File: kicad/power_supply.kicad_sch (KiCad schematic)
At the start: 2 parts

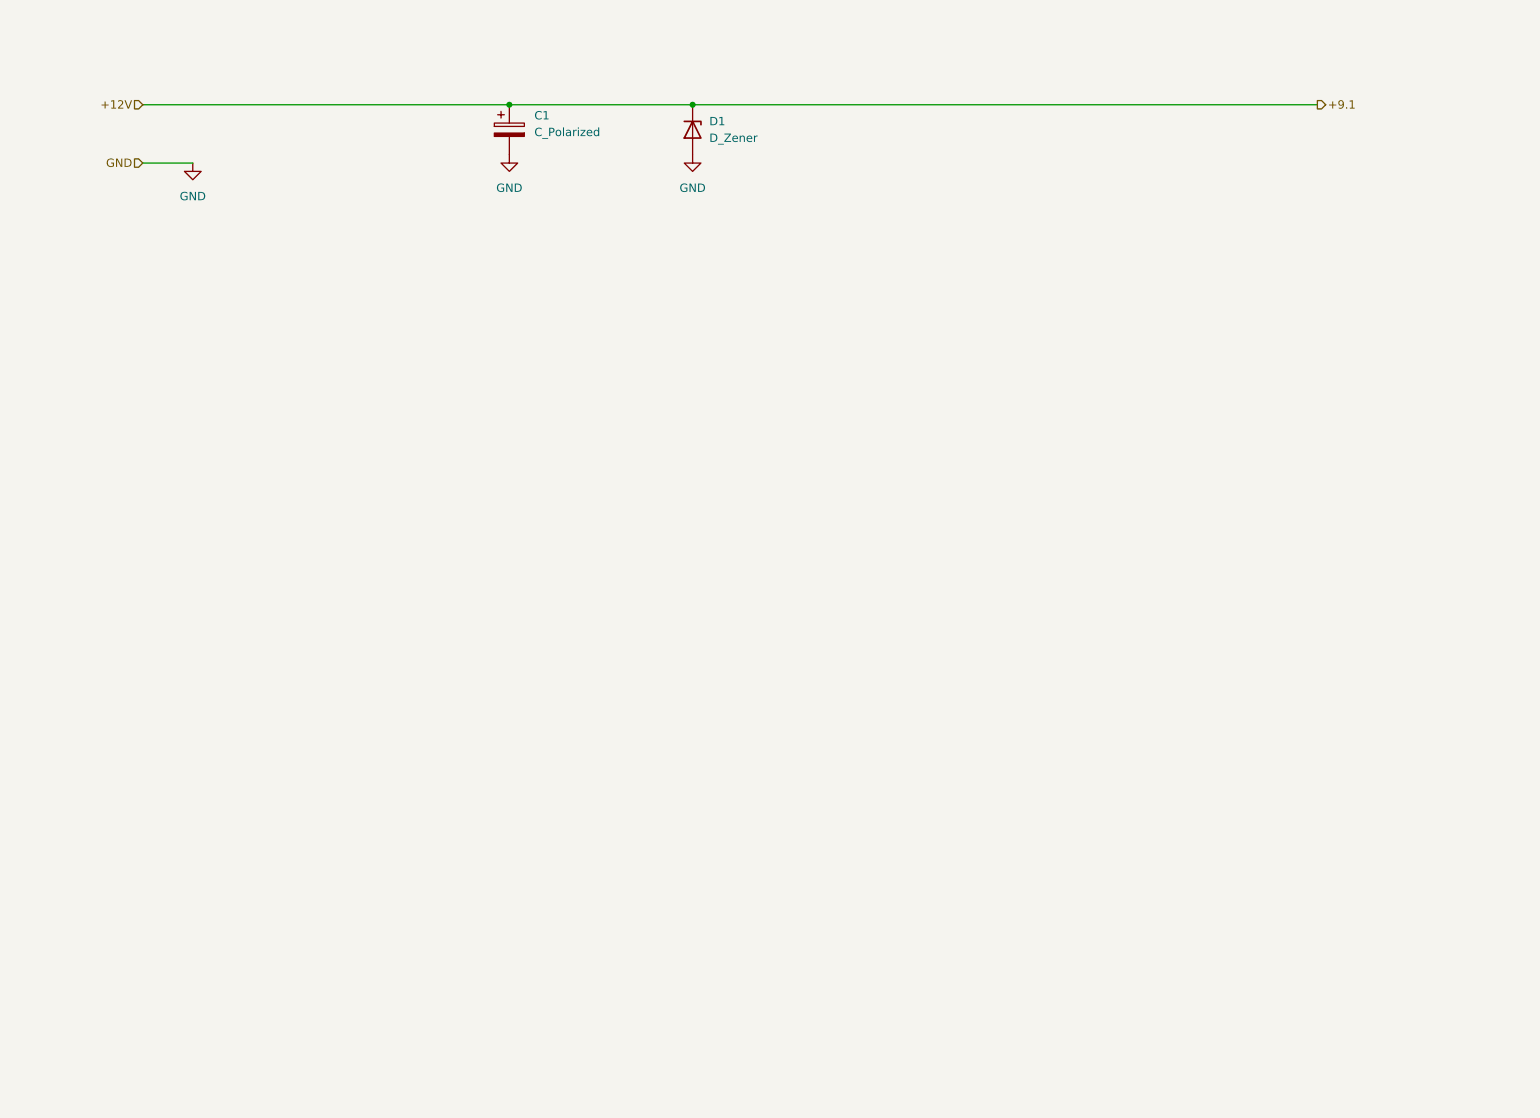
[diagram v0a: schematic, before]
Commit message: modificato lo schema della power supply aggiungendo più LM78xx per le varie tensioni
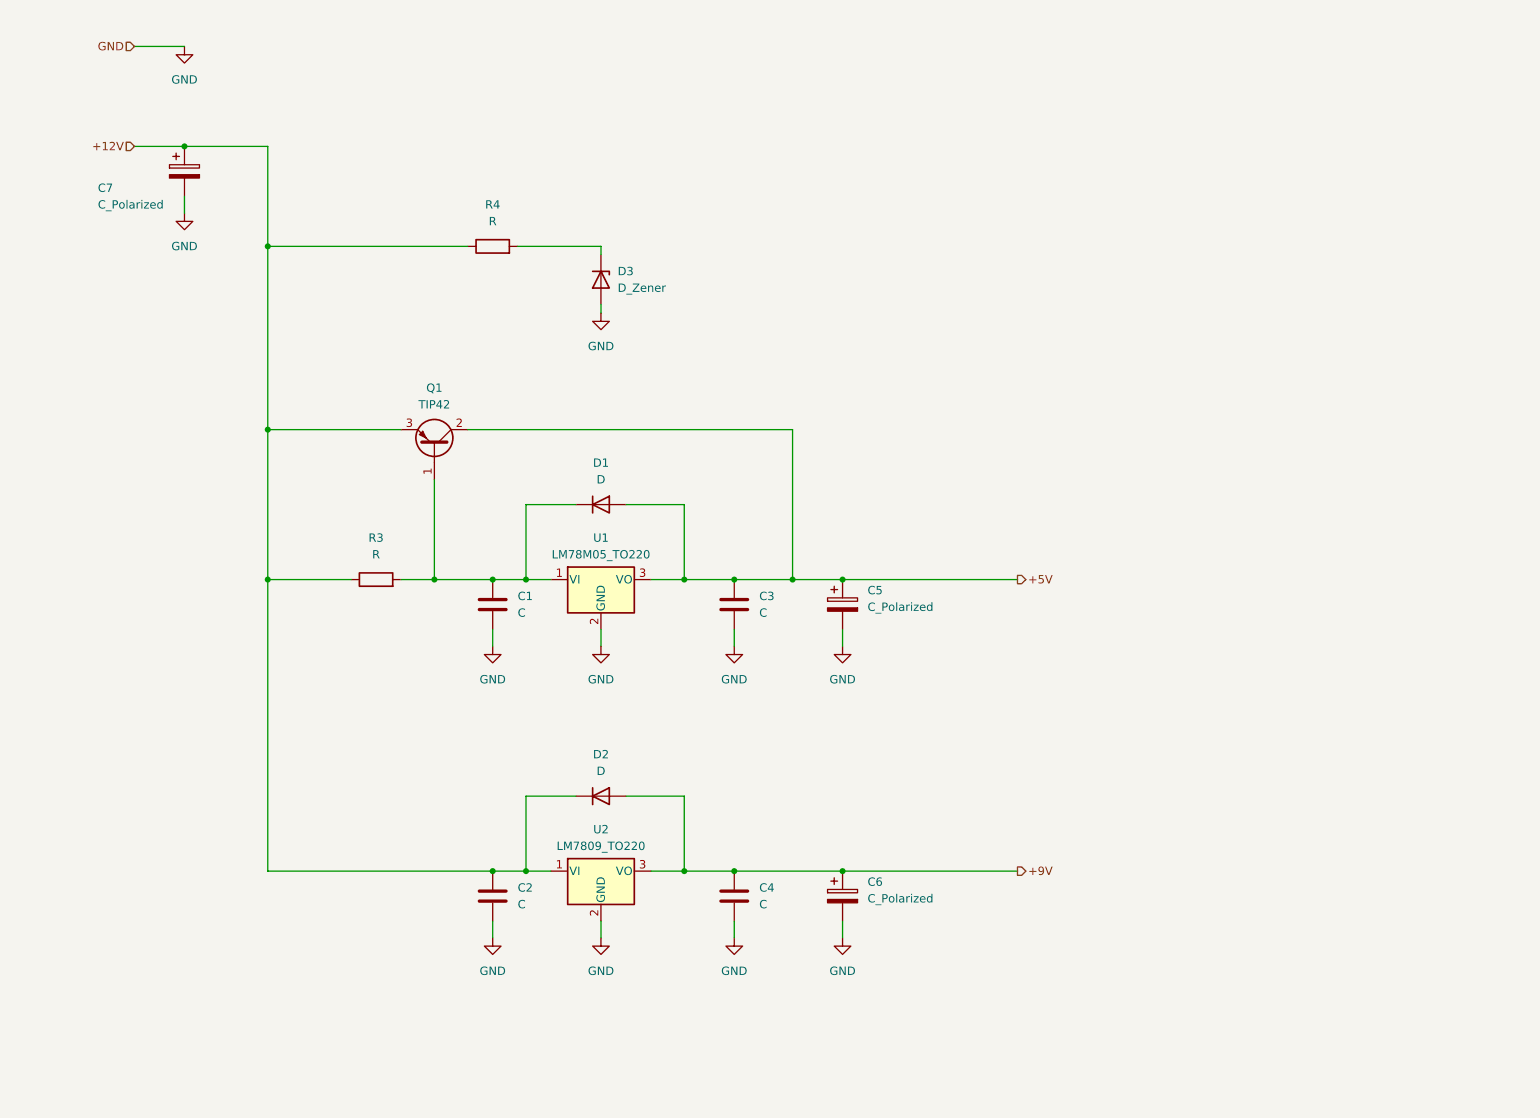
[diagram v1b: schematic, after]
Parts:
- removed C1: C_Polarized, symbol Device:C_Polarized
- removed D1: D_Zener, symbol Device:D_Zener
- added C1, C2, C3, C4: C, symbol Device:C
- added C5, C6, C7: C_Polarized, symbol Device:C_Polarized
- added D1, D2: D, symbol Device:D
- added D3: D_Zener, symbol Device:D_Zener
- added Q1: TIP42, Package_TO_SOT_THT:TO-220-3_Vertical, symbol Transistor_BJT:TIP42
- added R3, R4: R, symbol Device:R
- added U1: LM78M05_TO220, Package_TO_SOT_THT:TO-220-3_Vertical, symbol Regulator_Linear:LM78M05_TO220
- added U2: LM7809_TO220, Package_TO_SOT_THT:TO-220-3_Vertical, symbol Regulator_Linear:LM7809_TO220
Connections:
- net +12V: now also C2.1, C7.1, D2.1 (K), Q1.3 (E), R3.1, R4.1, U2.1 (VI)
- net GND: now also C1.2, C2.2, C3.2, C4.2, C5.2, C6.2, C7.2, D3.2 (A), U1.2 (GND), U2.2 (GND)
- new net: C1.1, D1.1 (K), Q1.1 (B), R3.2, U1.1 (VI)
- new net: D3.1 (K), R4.2
- new net +5V: C3.1, C5.1, D1.2 (A), Q1.2 (C), U1.3 (VO)
- new net +9V: C4.1, C6.1, D2.2 (A), U2.3 (VO)

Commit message: migliorato power supply schema aggiungendo zener e LM317 regolabile. aggiunto anche i calcoli.
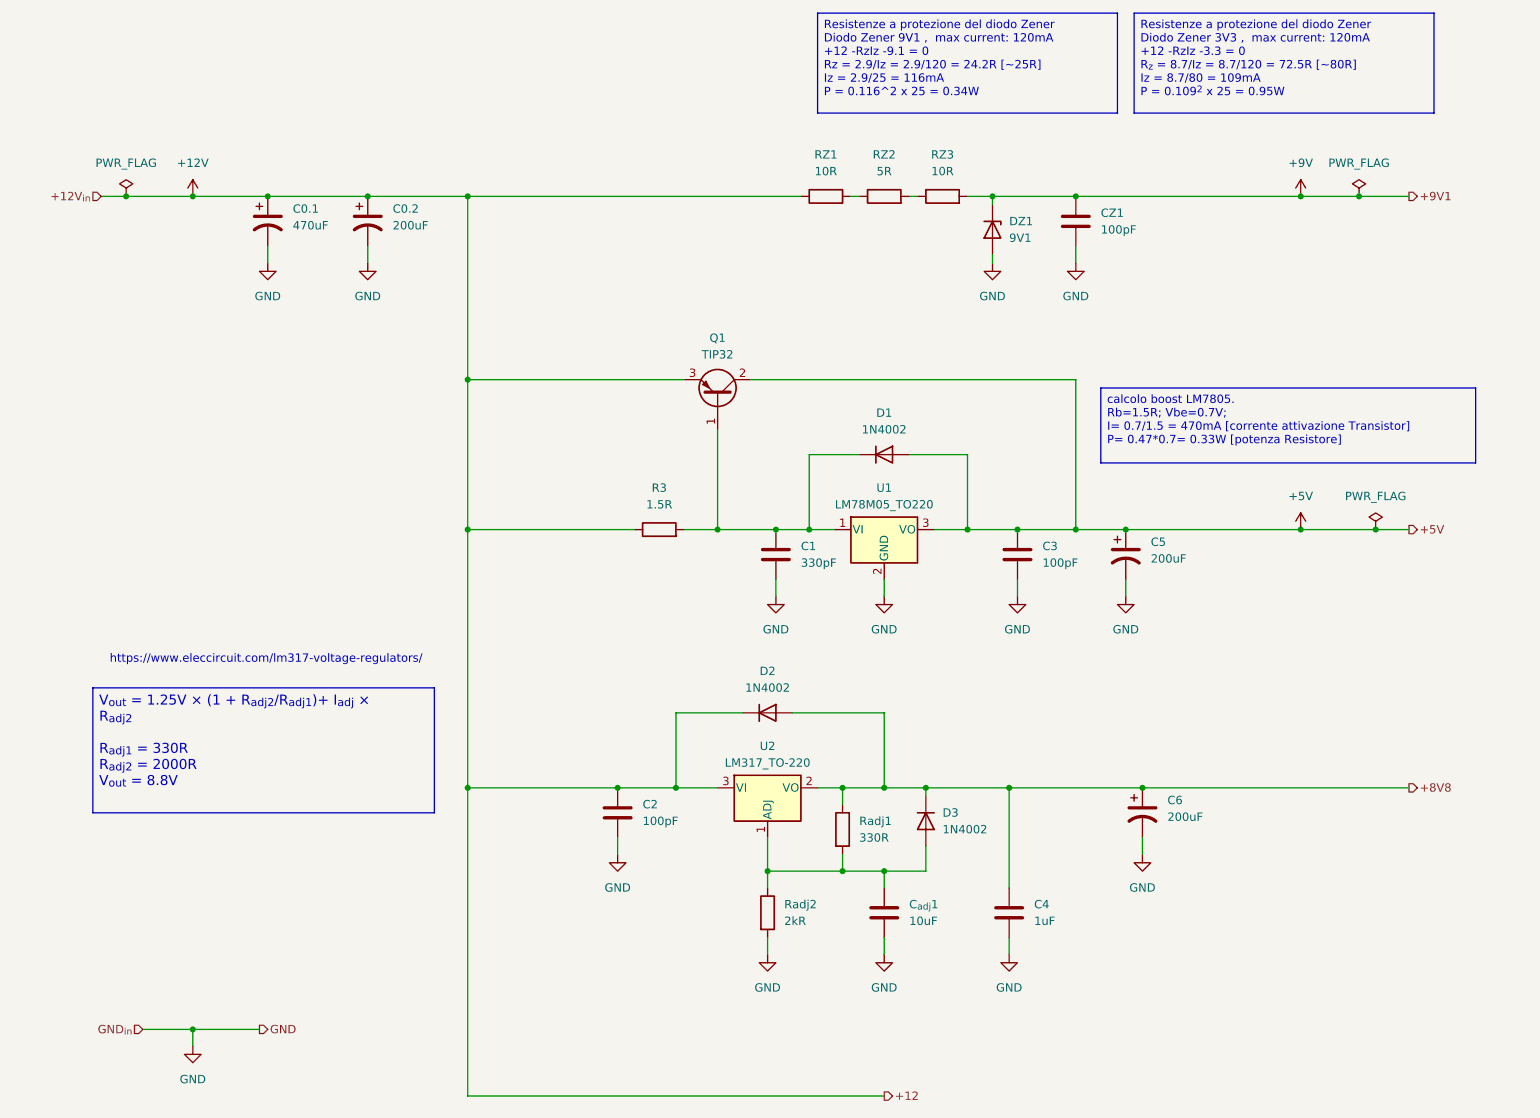
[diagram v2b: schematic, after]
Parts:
- removed C7: C_Polarized, symbol Device:C_Polarized
- removed U2: LM7809_TO220, Package_TO_SOT_THT:TO-220-3_Vertical, symbol Regulator_Linear:LM7809_TO220
- added C0.1: 470uF, symbol Device:C_Polarized_US
- added C0.2: 200uF, symbol Device:C_Polarized_US
- added CZ1: 100pF, symbol Device:C
- added C_{adj}1: 10uF, symbol Device:C
- added D3: 1N4002, Diode_THT:D_DO-15_P12.70mm_Horizontal, symbol Device:D
- added RZ1, RZ3: 10R, symbol Device:R
- added Radj1: 330R, symbol Device:R
- added Radj2: 2kR, symbol Device:R
- added U2: LM317_TO-220, Package_TO_SOT_THT:TO-220-3_Vertical, symbol Regulator_Linear:LM317_TO-220
- C1: value C -> 330pF
- C2, C3: value C -> 100pF
- C4: value C -> 1uF
- C5, C6: value C_Polarized -> 200uF; symbol Device:C_Polarized -> Device:C_Polarized_US
- D1, D2: value D -> 1N4002; footprint (none) -> Diode_THT:D_DO-15_P12.70mm_Horizontal
- DZ1: renamed from D3; value D_Zener -> 9V1
- Q1: value TIP42 -> TIP32
- R3: value R -> 1.5R
- RZ2: renamed from R4; value R -> 5R
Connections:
- net +12V: now also C0.1.1, C0.2.1, RZ1.1, U2.3 (VI); no longer RZ2.1
- net +9V: now also DZ1.1 (K), CZ1.1, RZ3.2; no longer C4.1, C6.1, D2.2 (A)
- net GND: now also C0.1.2, C0.2.2, CZ1.2, C_{adj}1.2, Radj2.2
- net at RZ2.2: now also RZ3.1; no longer DZ1.1 (K)
- new net: C_{adj}1.1, D3.2 (A), Radj1.2, Radj2.1, U2.1 (ADJ)
- new net: RZ1.2, RZ2.1
- new net +8V8: C4.1, C6.1, D2.2 (A), D3.1 (K), Radj1.1, U2.2 (VO)
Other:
- note added: "https://www.eleccircuit.com/lm317-voltage-regulators/"
- moved on the sheet: C1, C2, C3, C4, D1, D2, DZ1, Q1, R3, RZ2, U1
